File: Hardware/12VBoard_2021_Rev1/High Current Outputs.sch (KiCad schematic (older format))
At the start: 4 parts

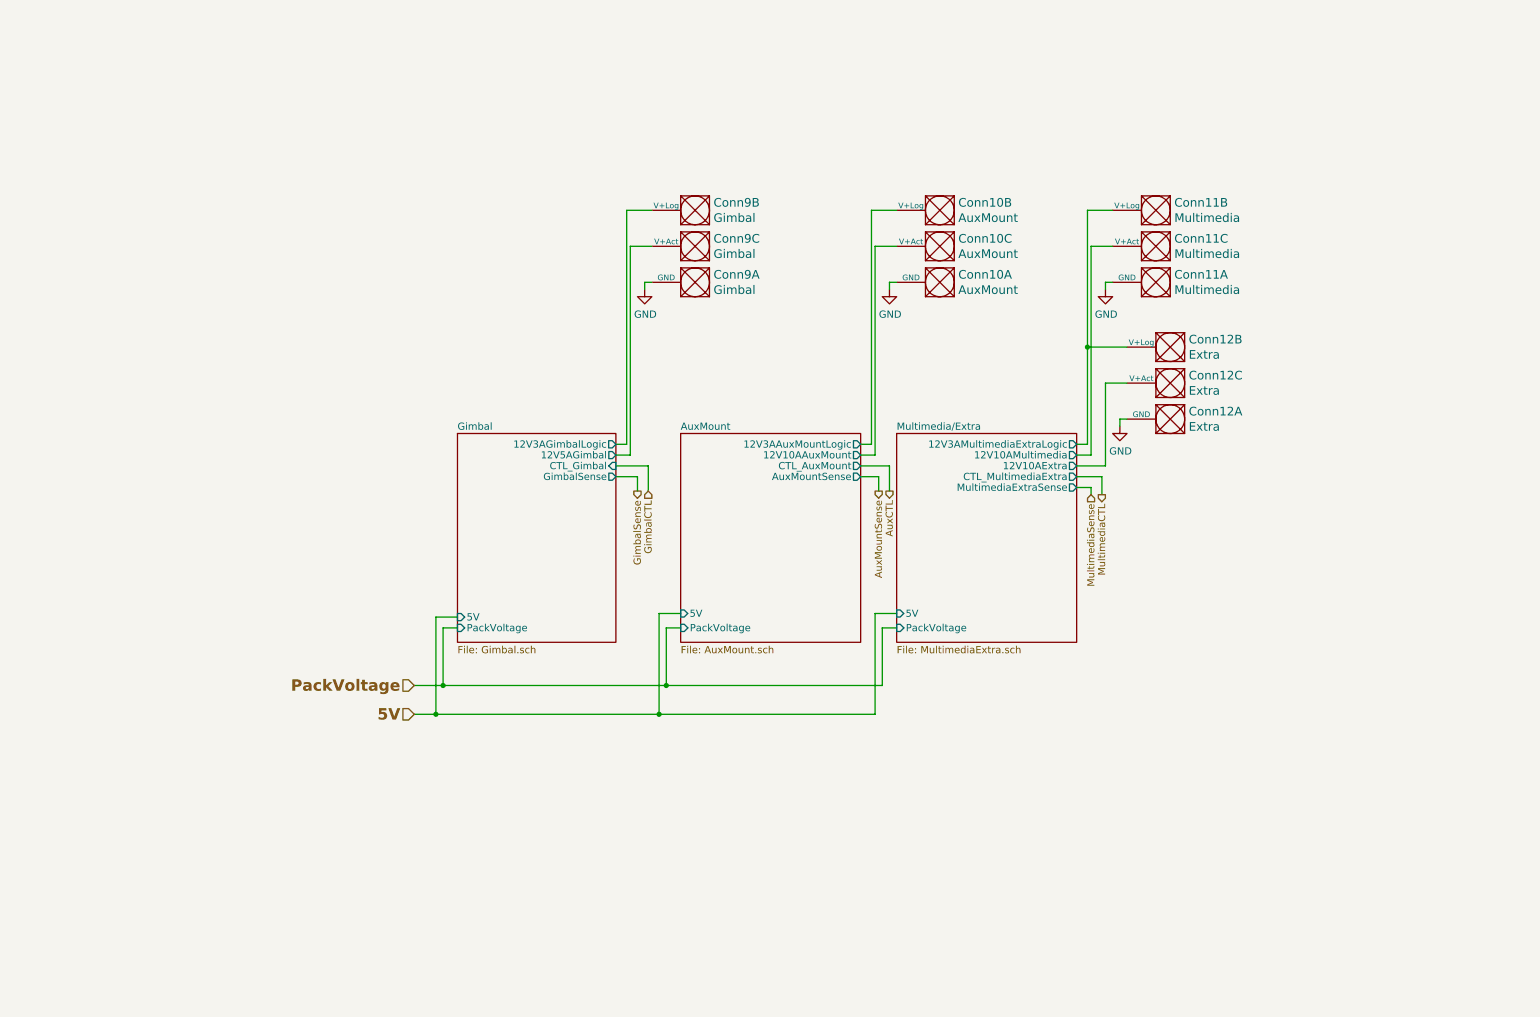
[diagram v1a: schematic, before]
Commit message: Aded oki and started change of high side logic setup
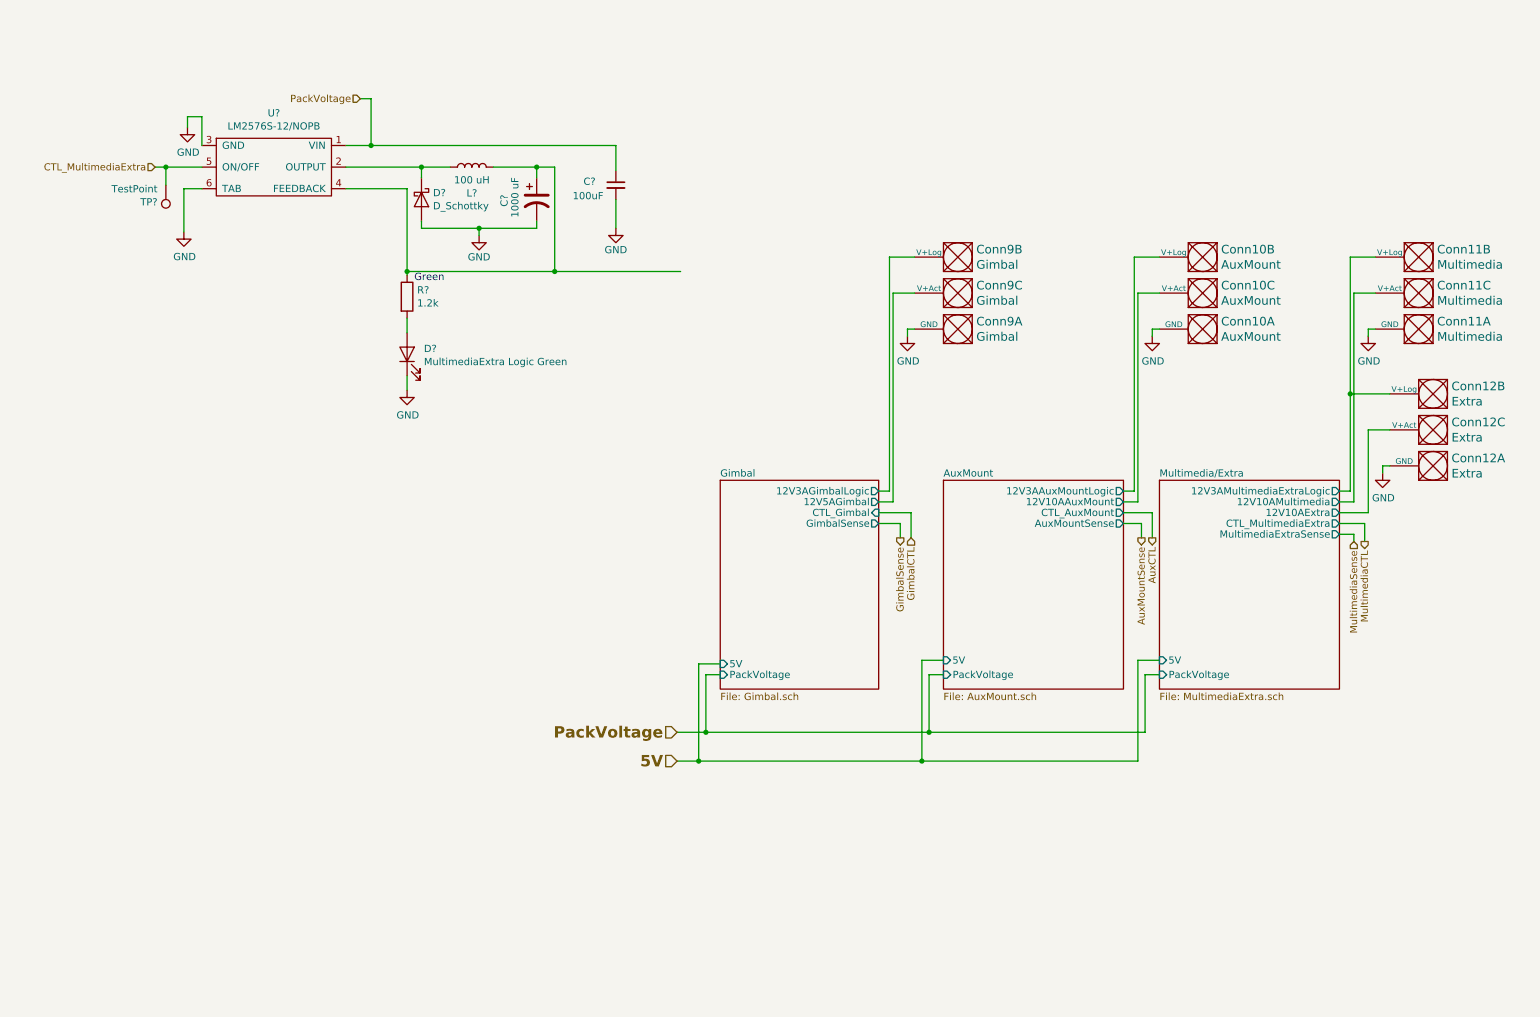
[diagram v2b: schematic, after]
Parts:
- added C?: 100uF, Capacitor_SMD:C_0603_1608Metric_Pad1.05x0.95mm_HandSolder, symbol Device:C_Small
- added C?: 1000 uF, Capacitor_THT:CP_Radial_D10.0mm_P5.00mm, symbol Device:CP1
- added D?: D_Schottky, Diode_THT:D_DO-201AD_P5.08mm_Vertical_KathodeUp, symbol Device:D_Schottky
- added D?: MultimediaExtra Logic Green, Diode_SMD:D_0603_1608Metric_Pad1.05x0.95mm_HandSolder, symbol Device:LED
- added L?: 100 uH, Inductor_SMD:L_0603_1608Metric_Pad1.05x0.95mm_HandSolder, symbol Device:L
- added R?: 1.2k, Resistor_SMD:R_0603_1608Metric_Pad1.05x0.95mm_HandSolder, symbol Device:R
- added TP?: TestPoint, TestPoint:TestPoint_Pad_2.5x2.5mm, symbol Connector:TestPoint
- added U?: LM2576S-12/NOPB, MRDT_Devices:LM2576, symbol 12VBoard_2021_Rev1-rescue:LM2576D2TR4-MRDT_Devices
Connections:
- net GND: now also C?.2, C?.2, D?.1 (K), D?.2 (A), U?.3 (GND), U?.6 (TAB)
- net PackVoltage: now also C?.1, U?.1 (VIN)
- new net: D?.1 (K), L?.1, U?.2 (OUTPUT)
- new net: C?.1, L?.2, R?.1, U?.4 (FEEDBACK)
- new net: D?.2 (A), R?.2
- new net CTL_MultimediaExtra: TP?.1, U?.5 (ON/OFF)
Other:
- note added: "Green"
- moved on the sheet: Conn10A, Conn10B, Conn10C, Conn11A, Conn11B, Conn11C, Conn12A, Conn12B, Conn12C, Conn9A, Conn9B, Conn9C

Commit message: Changes!
Added the new correct connectors and redid all signal lines to the High Current side of the board. Also deleted all uncessacary components on the High current side that are no longer used.
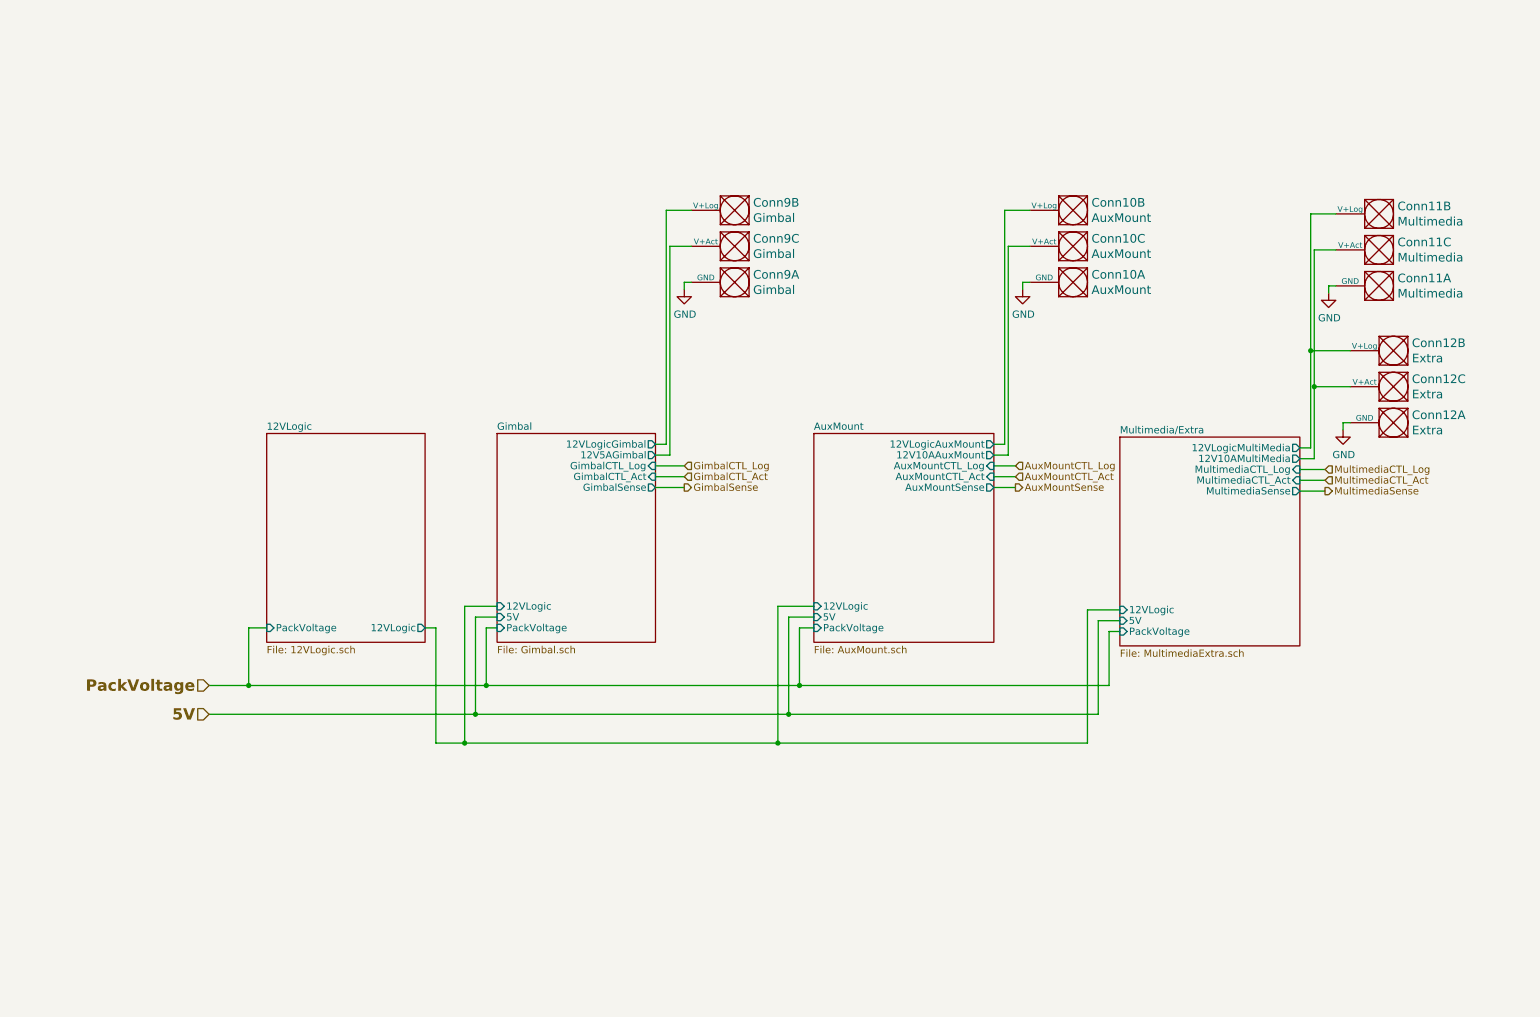
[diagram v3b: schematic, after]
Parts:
- removed C?: 100uF, Capacitor_SMD:C_0603_1608Metric_Pad1.05x0.95mm_HandSolder, symbol Device:C_Small
- removed C?: 1000 uF, Capacitor_THT:CP_Radial_D10.0mm_P5.00mm, symbol Device:CP1
- removed D?: D_Schottky, Diode_THT:D_DO-201AD_P5.08mm_Vertical_KathodeUp, symbol Device:D_Schottky
- removed D?: MultimediaExtra Logic Green, Diode_SMD:D_0603_1608Metric_Pad1.05x0.95mm_HandSolder, symbol Device:LED
- removed L?: 100 uH, Inductor_SMD:L_0603_1608Metric_Pad1.05x0.95mm_HandSolder, symbol Device:L
- removed R?: 1.2k, Resistor_SMD:R_0603_1608Metric_Pad1.05x0.95mm_HandSolder, symbol Device:R
- removed TP?: TestPoint, TestPoint:TestPoint_Pad_2.5x2.5mm, symbol Connector:TestPoint
- removed U?: LM2576S-12/NOPB, MRDT_Devices:LM2576, symbol 12VBoard_2021_Rev1-rescue:LM2576D2TR4-MRDT_Devices
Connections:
- net Multimedia/Extra/12V10AMultimedia is gone; now on net Multimedia/Extra/12V10AMultiMedia: Conn11.3 (V+Act)
- net AuxMount/12V3AAuxMountLogic renamed AuxMount/12VLogicAuxMount
- net Gimbal/12V3AGimbalLogic renamed Gimbal/12VLogicGimbal
- net Multimedia/Extra/12V10AExtra renamed Multimedia/Extra/12V10AMultiMedia
- net Multimedia/Extra/12V3AMultimediaExtraLogic renamed Multimedia/Extra/12VLogicMultiMedia
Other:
- note removed: "Green"
- moved on the sheet: Conn10A, Conn10B, Conn10C, Conn11A, Conn11B, Conn11C, Conn12A, Conn12B, Conn12C, Conn9A, Conn9B, Conn9C

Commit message: Layed out logic power
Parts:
- Conn10, Conn11, Conn12, Conn9: footprint MRDT_Connectors:Anderson_3_Horizontal_Side_by_Side -> MRDT_Connectors:Anderson_3_Vertical_Side_by_Side
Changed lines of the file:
@@
 F 0 "Conn10" H 7897 2422 60  0000 R CNN
 F 1 "AuxMount" H 7897 2528 60  0000 R CNN
-F 2 "MRDT_Connectors:Anderson_3_Horizontal_Side_by_Side" H 7775 1825 60  0001 C CNN
+F 2 "MRDT_Connectors:Anderson_3_Vertical_Side_by_Side" H 7775 1825 60  0001 C CNN
 F 3 "" H 7775 1825 60  0001 C CNN
 	1    7925 2375
@@
 F 0 "Conn10" H 7897 2172 60  0000 R CNN
 F 1 "AuxMount" H 7897 2278 60  0000 R CNN
-F 2 "MRDT_Connectors:Anderson_3_Horizontal_Side_by_Side" H 7775 1575 60  0001 C CNN
+F 2 "MRDT_Connectors:Anderson_3_Vertical_Side_by_Side" H 7775 1575 60  0001 C CNN
 F 3 "" H 7775 1575 60  0001 C CNN
 	3    7925 2125
@@
 F 0 "Conn11" H 10022 2447 60  0000 R CNN
 F 1 "Multimedia" H 10022 2553 60  0000 R CNN
-F 2 "MRDT_Connectors:Anderson_3_Horizontal_Side_by_Side" H 9900 1850 60  0001 C CNN
+F 2 "MRDT_Connectors:Anderson_3_Vertical_Side_by_Side" H 9900 1850 60  0001 C CNN
 F 3 "" H 9900 1850 60  0001 C CNN
 	1    10050 2400
@@
 F 0 "Conn11" H 10022 2197 60  0000 R CNN
 F 1 "Multimedia" H 10022 2303 60  0000 R CNN
-F 2 "MRDT_Connectors:Anderson_3_Horizontal_Side_by_Side" H 9900 1600 60  0001 C CNN
+F 2 "MRDT_Connectors:Anderson_3_Vertical_Side_by_Side" H 9900 1600 60  0001 C CNN
 F 3 "" H 9900 1600 60  0001 C CNN
 	3    10050 2150
@@
 F 0 "Conn12" H 10122 3397 60  0000 R CNN
 F 1 "Extra" H 10122 3503 60  0000 R CNN
-F 2 "MRDT_Connectors:Anderson_3_Horizontal_Side_by_Side" H 10000 2800 60  0001 C CNN
+F 2 "MRDT_Connectors:Anderson_3_Vertical_Side_by_Side" H 10000 2800 60  0001 C CNN
 F 3 "" H 10000 2800 60  0001 C CNN
 	1    10150 3350
@@
 F 0 "Conn12" H 10122 3147 60  0000 R CNN
 F 1 "Extra" H 10122 3253 60  0000 R CNN
-F 2 "MRDT_Connectors:Anderson_3_Horizontal_Side_by_Side" H 10000 2550 60  0001 C CNN
+F 2 "MRDT_Connectors:Anderson_3_Vertical_Side_by_Side" H 10000 2550 60  0001 C CNN
 F 3 "" H 10000 2550 60  0001 C CNN
 	3    10150 3100
@@
 F 0 "Conn9" H 5547 2422 60  0000 R CNN
 F 1 "Gimbal" H 5547 2528 60  0000 R CNN
-F 2 "MRDT_Connectors:Anderson_3_Horizontal_Side_by_Side" H 5425 1825 60  0001 C CNN
+F 2 "MRDT_Connectors:Anderson_3_Vertical_Side_by_Side" H 5425 1825 60  0001 C CNN
 F 3 "" H 5425 1825 60  0001 C CNN
 	1    5575 2375
@@
 F 0 "Conn9" H 5547 2172 60  0000 R CNN
 F 1 "Gimbal" H 5547 2278 60  0000 R CNN
-F 2 "MRDT_Connectors:Anderson_3_Horizontal_Side_by_Side" H 5425 1575 60  0001 C CNN
+F 2 "MRDT_Connectors:Anderson_3_Vertical_Side_by_Side" H 5425 1575 60  0001 C CNN
 F 3 "" H 5425 1575 60  0001 C CNN
 	3    5575 2125
@@
 F 0 "Conn9" H 5547 1922 60  0000 R CNN
 F 1 "Gimbal" H 5547 2028 60  0000 R CNN
-F 2 "MRDT_Connectors:Anderson_3_Horizontal_Side_by_Side" H 5425 1325 60  0001 C CNN
+F 2 "MRDT_Connectors:Anderson_3_Vertical_Side_by_Side" H 5425 1325 60  0001 C CNN
 F 3 "" H 5425 1325 60  0001 C CNN
 	2    5575 1875
@@
 F 0 "Conn10" H 7897 1922 60  0000 R CNN
 F 1 "AuxMount" H 7897 2028 60  0000 R CNN
-F 2 "MRDT_Connectors:Anderson_3_Horizontal_Side_by_Side" H 7775 1325 60  0001 C CNN
+F 2 "MRDT_Connectors:Anderson_3_Vertical_Side_by_Side" H 7775 1325 60  0001 C CNN
 F 3 "" H 7775 1325 60  0001 C CNN
 	2    7925 1875
@@
 F 0 "Conn11" H 10022 1947 60  0000 R CNN
 F 1 "Multimedia" H 10022 2053 60  0000 R CNN
-F 2 "MRDT_Connectors:Anderson_3_Horizontal_Side_by_Side" H 9900 1350 60  0001 C CNN
+F 2 "MRDT_Connectors:Anderson_3_Vertical_Side_by_Side" H 9900 1350 60  0001 C CNN
 F 3 "" H 9900 1350 60  0001 C CNN
 	2    10050 1900
@@
 F 0 "Conn12" H 10122 2897 60  0000 R CNN
 F 1 "Extra" H 10122 3003 60  0000 R CNN
-F 2 "MRDT_Connectors:Anderson_3_Horizontal_Side_by_Side" H 10000 2300 60  0001 C CNN
+F 2 "MRDT_Connectors:Anderson_3_Vertical_Side_by_Side" H 10000 2300 60  0001 C CNN
 F 3 "" H 10000 2300 60  0001 C CNN
 	2    10150 2850

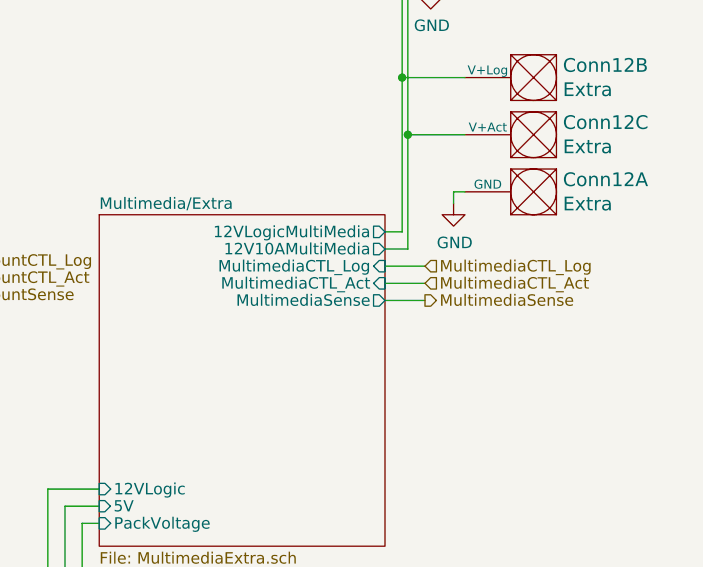
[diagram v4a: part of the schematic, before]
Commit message: Added all logic circuits for high current
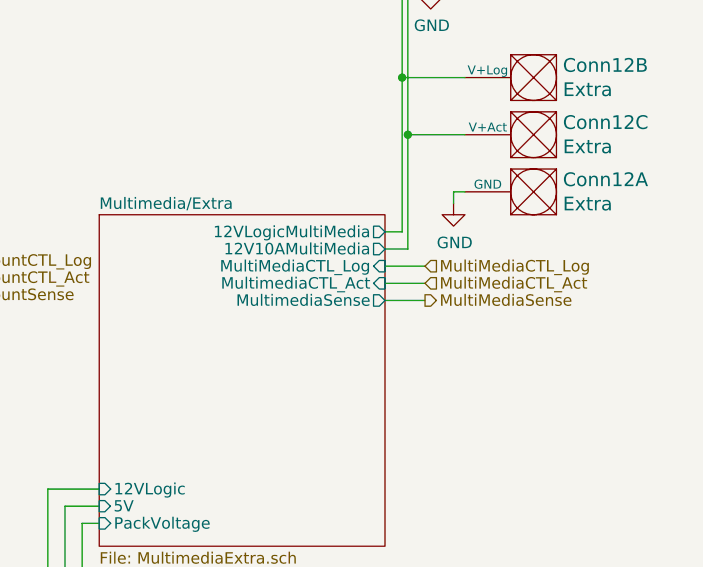
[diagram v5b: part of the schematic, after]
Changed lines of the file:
@@
 F7 "PackVoltage" I L 8150 4900 50
 F8 "12VLogic" I L 8150 4750 50
-F9 "MultimediaCTL_Log" I R 9400 3775 50
+F9 "MultiMediaCTL_Log" I R 9400 3775 50
 $EndSheet
 Wire Wire Line
@@
 AuxMountSense
 Text HLabel 9575 3775 2    50   Input ~ 0
-MultimediaCTL_Log
+MultiMediaCTL_Log
 Text HLabel 9575 3850 2    50   Input ~ 0
-MultimediaCTL_Act
+MultiMediaCTL_Act
 Text HLabel 9575 3925 2    50   Output ~ 0
-MultimediaSense
+MultiMediaSense
 Wire Wire Line
 	9400 3775 9575 3775
